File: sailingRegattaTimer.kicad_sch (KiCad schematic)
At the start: 25 parts, among them J1-Red-1M1 Conn_01x02_Socket, J10-12v-In1 Conn_01x02_Socket, J2-Yel-2M1 Conn_01x02_Socket, J3-Grn-3M1 J3-Grn-3M, J4-Blu-5M1 J4-Blu-5M1, J5-5v-LED1 Conn_01x02_Socket, J6-Reset1 J6-Reset, J7-Ext-Buz1 Conn_01x02_Socket, J8-Pololu-VReg1 Conn_01x04_Socket, J9-Relay1 Conn_01x03_Socket

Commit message: initial commit - schematic and pcb
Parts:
- removed R1: R1, Resistor_THT:R_Axial_DIN0204_L3.6mm_D1.6mm_P1.90mm_Vertical, symbol Device:R
- removed R2, R3, R4: R, Resistor_THT:R_Axial_DIN0204_L3.6mm_D1.6mm_P1.90mm_Vertical, symbol Device:R
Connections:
- net +5V: no longer J1-Red-1M1.1 (Pin_1), J2-Yel-2M1.1 (Pin_1), J3-Grn-3M1.1 (Pin_1), J4-Blu-5M1.1 (Pin_1), SW1-Red-1M1.1, SW2-Yel-2M1.1, SW3-Grn-3M1.1, SW4-Blu-5M1.1
- net GND: now also J1-Red-1M1.1 (Pin_1), J2-Yel-2M1.1 (Pin_1), J3-Grn-3M1.1 (Pin_1), J4-Blu-5M1.1 (Pin_1), SW1-Red-1M1.1, SW2-Yel-2M1.1, SW3-Grn-3M1.1, SW4-Blu-5M1.1

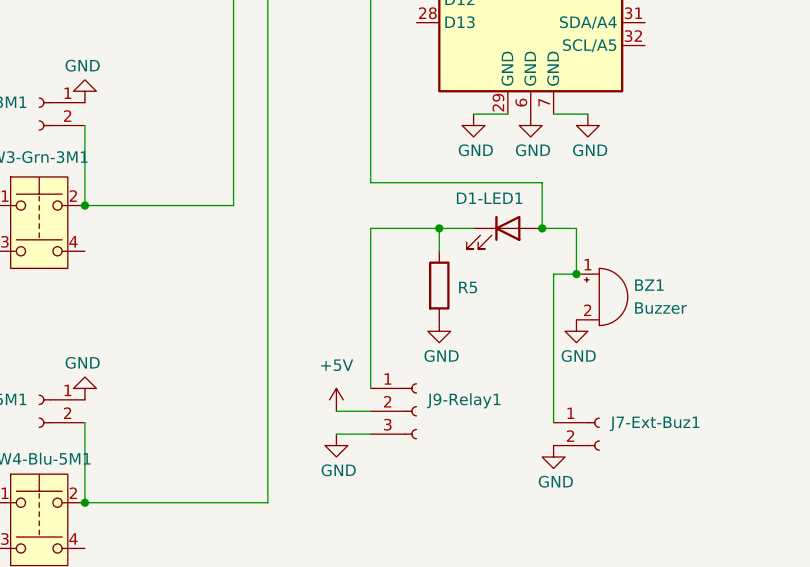
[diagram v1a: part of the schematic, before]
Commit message: add relay and other labels
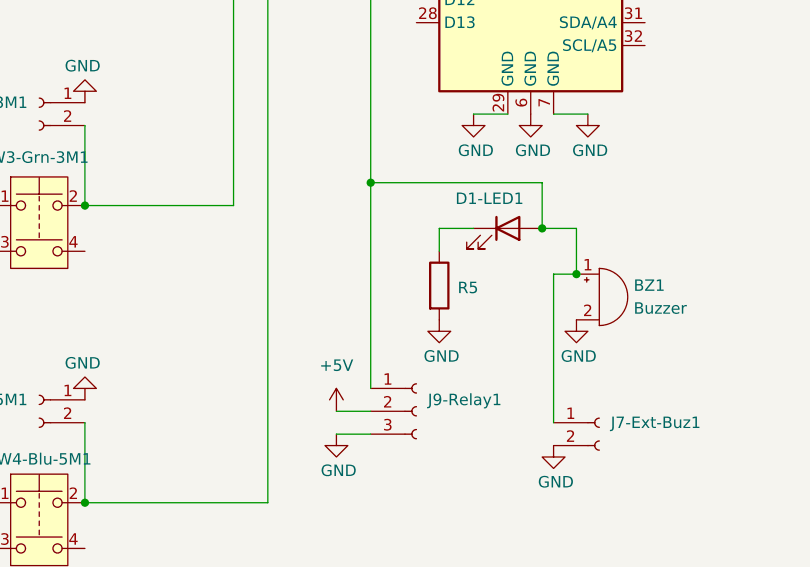
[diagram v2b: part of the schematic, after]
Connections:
- net at D1-LED1.1 (K), R5.1: no longer J9-Relay1.1 (Pin_1)
- net at A1.19 (D4), BZ1.1 (+), D1-LED1.2 (A)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: now also J9-Relay1.1 (Pin_1)
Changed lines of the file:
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@@
 	)
 	(junction
-		(at 179.07 128.27)
+		(at 171.45 123.19)
 		(diameter 0)
 		(color 0 0 0 0)
@@
 	(wire
 		(pts
-			(xy 171.45 128.27) (xy 179.07 128.27)
-		)
-		(stroke
-			(width 0)
-			(type default)
-		)
-	)
-	(wire
-		(pts
 			(xy 195.58 115.57) (xy 191.77 115.57)
 		)
@@
 	(wire
 		(pts
+			(xy 171.45 123.19) (xy 171.45 146.05)
+		)
+		(stroke
+			(width 0)
+			(type default)
+		)
+	)
+	(wire
+		(pts
 			(xy 222.25 54.61) (xy 224.79 54.61)
 		)
@@
 		)
 	)
-	(wire
-		(pts
-			(xy 171.45 128.27) (xy 171.45 146.05)
-		)
-		(stroke
-			(width 0)
-			(type default)
-		)
-	)
 	(symbol
 		(lib_id "Connector:Conn_01x04_Socket")
@@
 		)
 		(instances
-			(project ""
+			(project "sailingRegattaTimer"
 				(path "/e63e39d7-6ac0-4ffd-8aa3-1841a4541b55"
 					(reference "J8-Pololu-VReg1")
@@
 		)
 		(instances
-			(project ""
+			(project "sailingRegattaTimer"
 				(path "/e63e39d7-6ac0-4ffd-8aa3-1841a4541b55"
 					(reference "J9-Relay1")
@@
 		)
 		(instances
-			(project ""
+			(project "sailingRegattaTimer"
 				(path "/e63e39d7-6ac0-4ffd-8aa3-1841a4541b55"
 					(reference "J4-Blu-5M1")
@@
 		)
 		(instances
-			(project "kicad"
+			(project "sailingRegattaTimer"
 				(path "/e63e39d7-6ac0-4ffd-8aa3-1841a4541b55"
 					(reference "SW3-Grn-3M1")
@@
 		)
 		(instances
-			(project ""
+			(project "sailingRegattaTimer"
 				(path "/e63e39d7-6ac0-4ffd-8aa3-1841a4541b55"
 					(reference "D1-LED1")
@@
 		)
 		(instances
-			(project ""
+			(project "sailingRegattaTimer"
 				(path "/e63e39d7-6ac0-4ffd-8aa3-1841a4541b55"
 					(reference "A1")
@@
 		)
 		(instances
-			(project ""
+			(project "sailingRegattaTimer"
 				(path "/e63e39d7-6ac0-4ffd-8aa3-1841a4541b55"
 					(reference "J6-Reset1")
@@
 		)
 		(instances
-			(project "kicad"
+			(project "sailingRegattaTimer"
 				(path "/e63e39d7-6ac0-4ffd-8aa3-1841a4541b55"
 					(reference "SW2-Yel-2M1")
@@
 		)
 		(instances
-			(project ""
+			(project "sailingRegattaTimer"
 				(path "/e63e39d7-6ac0-4ffd-8aa3-1841a4541b55"
 					(reference "J1-Red-1M1")
@@
 		)
 		(instances
-			(project ""
+			(project "sailingRegattaTimer"
 				(path "/e63e39d7-6ac0-4ffd-8aa3-1841a4541b55"
 					(reference "#PWR06")
@@
 		)
 		(instances
-			(project "kicad"
+			(project "sailingRegattaTimer"
 				(path "/e63e39d7-6ac0-4ffd-8aa3-1841a4541b55"
 					(reference "R5")
@@
 		)
 		(instances
-			(project ""
+			(project "sailingRegattaTimer"
 				(path "/e63e39d7-6ac0-4ffd-8aa3-1841a4541b55"
 					(reference "BZ1")
@@
 		)
 		(instances
-			(project ""
+			(project "sailingRegattaTimer"
 				(path "/e63e39d7-6ac0-4ffd-8aa3-1841a4541b55"
 					(reference "J2-Yel-2M1")
@@
 		)
 		(instances
-			(project ""
+			(project "sailingRegattaTimer"
 				(path "/e63e39d7-6ac0-4ffd-8aa3-1841a4541b55"
 					(reference "SW1-Red-1M1")
@@
 		)
 		(instances
-			(project ""
+			(project "sailingRegattaTimer"
 				(path "/e63e39d7-6ac0-4ffd-8aa3-1841a4541b55"
 					(reference "J5-5v-LED1")
@@
 		)
 		(instances
-			(project "kicad"
+			(project "sailingRegattaTimer"
 				(path "/e63e39d7-6ac0-4ffd-8aa3-1841a4541b55"
 					(reference "SW4-Blu-5M1")
